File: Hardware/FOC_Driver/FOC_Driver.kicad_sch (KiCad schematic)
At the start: 0 parts

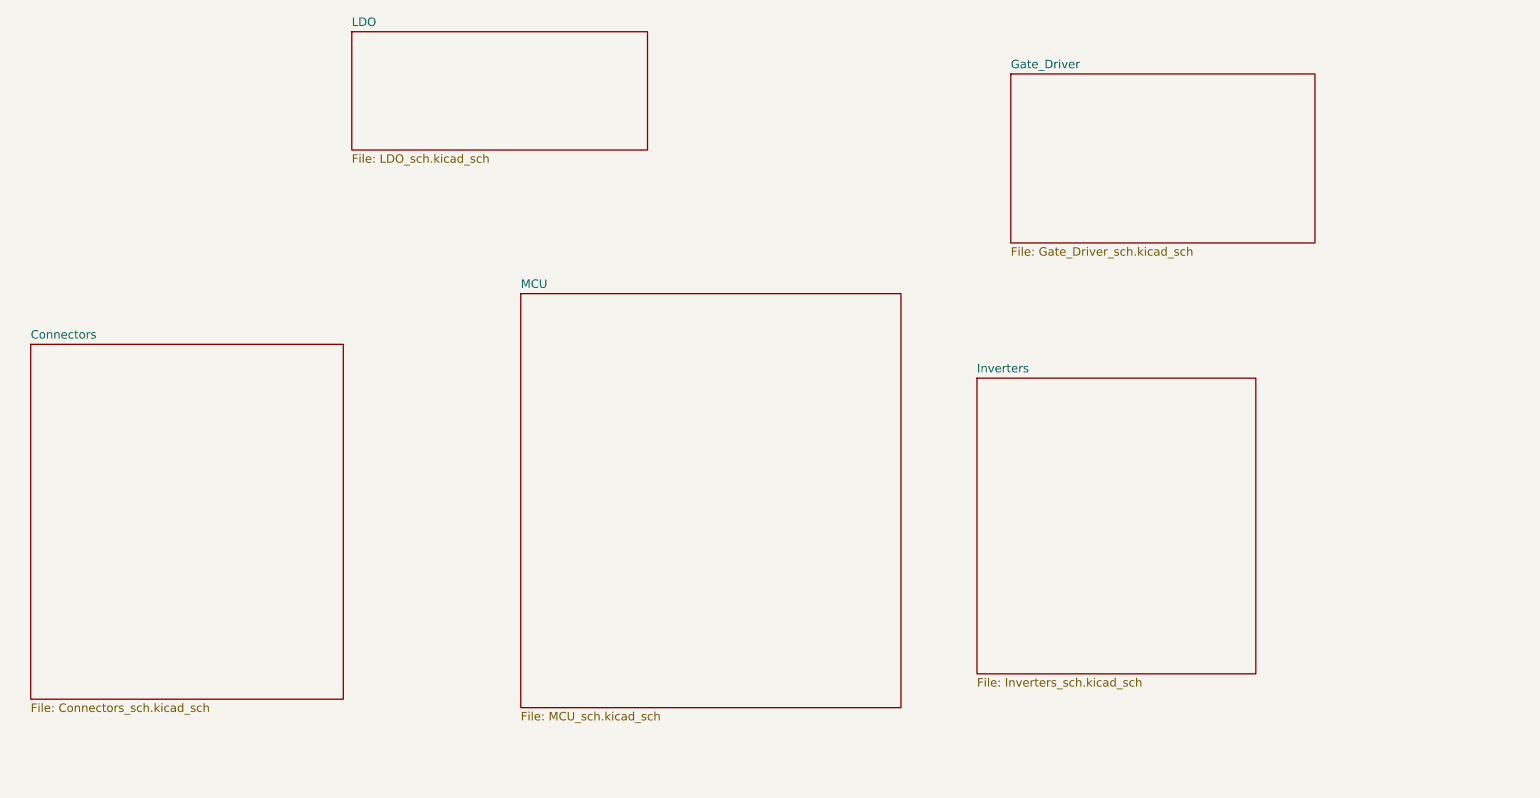
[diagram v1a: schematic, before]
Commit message: schematic completed
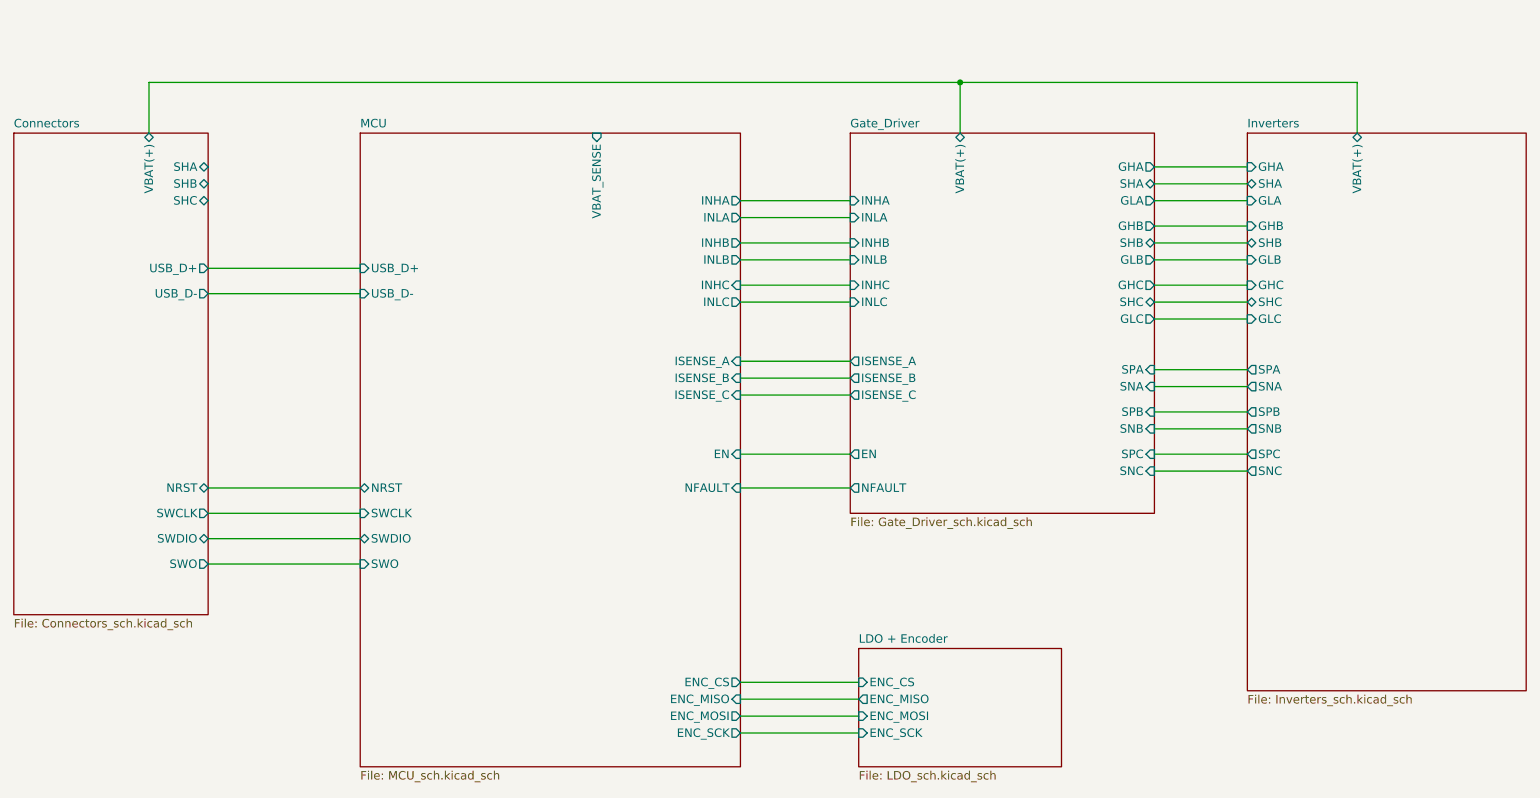
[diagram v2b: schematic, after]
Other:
- sheet LDO renamed LDO + Encoder
- sheet Connectors ports: added NRST, SHA, SHB, SHC, SWCLK, SWDIO, SWO, USB_D+, USB_D-, VBAT(+); removed none
- sheet Gate_Driver ports: added EN, GHA, GHB, GHC, GLA, GLB, GLC, INHA, INHB, INHC, INLA, INLB, INLC, ISENSE_A, ISENSE_B, ISENSE_C, NFAULT, SHA, SHB, SHC, SNA, SNB, SNC, SPA, SPB, SPC, VBAT(+); removed none
- sheet Inverters ports: added GHA, GHB, GHC, GLA, GLB, GLC, SHA, SHB, SHC, SNA, SNB, SNC, SPA, SPB, SPC, VBAT(+); removed none
- sheet LDO + Encoder ports: added ENC_CS, ENC_MISO, ENC_MOSI, ENC_SCK; removed none
- sheet MCU ports: added EN, ENC_CS, ENC_MISO, ENC_MOSI, ENC_SCK, INHA, INHB, INHC, INLA, INLB, INLC, ISENSE_A, ISENSE_B, ISENSE_C, NFAULT, NRST, SWCLK, SWDIO, SWO, USB_D+, USB_D-, VBAT_SENSE; removed none

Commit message: Schematic update, XT30/MR30 connectors and PCB layout in progress
- Connectors: AMASS XT30PW and MR30PW from Kicad_Libs (eConnector)
- Schematic updates on main, MCU and gate driver sheets
- PCB: footprints placed, routing in progress
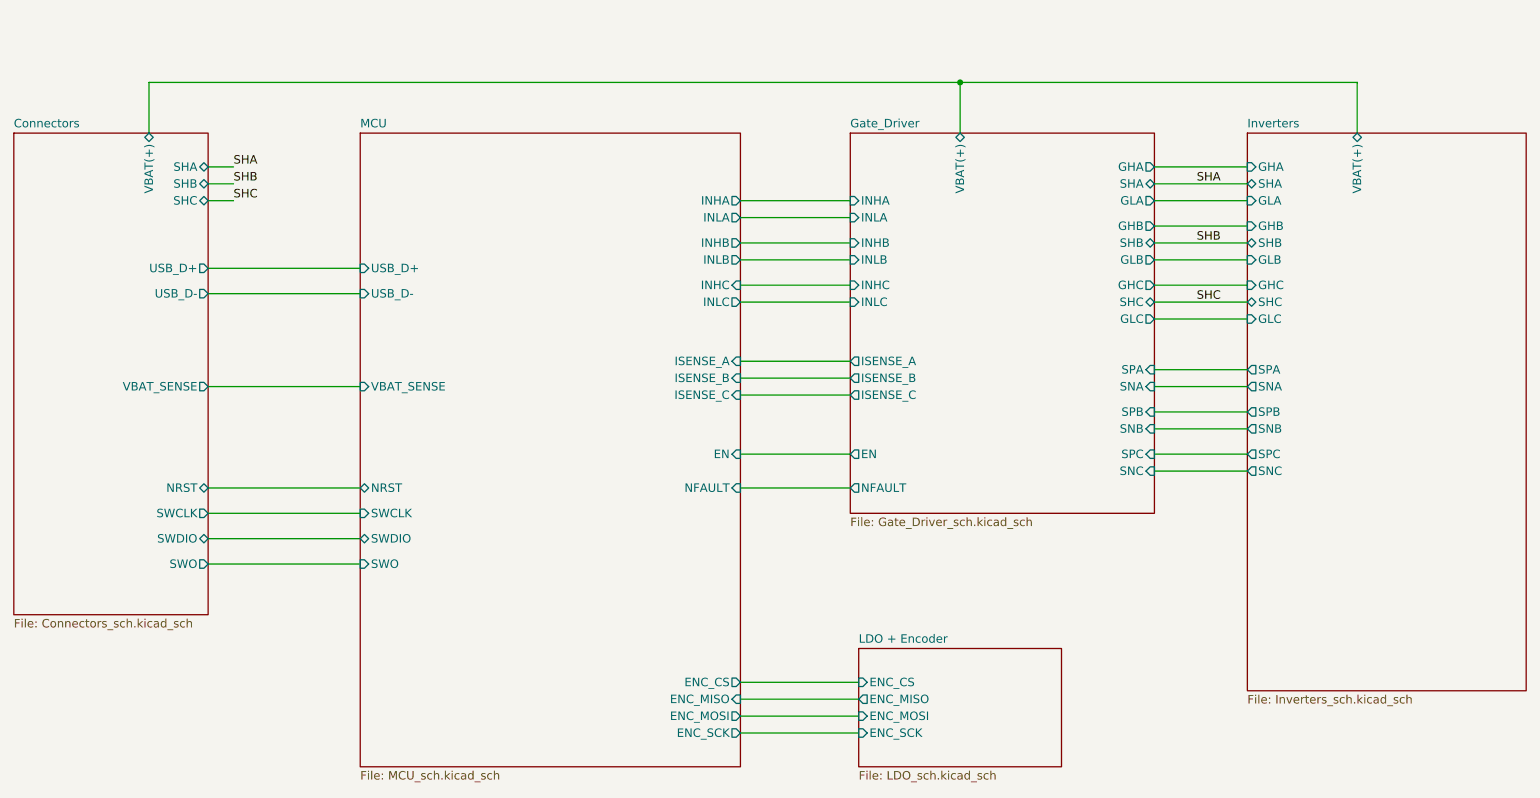
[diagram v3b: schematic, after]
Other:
- sheet Connectors ports: added VBAT_SENSE; removed none
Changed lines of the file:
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@@
 	(wire
 		(pts
+			(xy 63.5 85.09) (xy 86.36 85.09)
+		)
+		(stroke
+			(width 0)
+			(type default)
+		)
+	)
+	(wire
+		(pts
 			(xy 205.74 57.15) (xy 219.71 57.15)
 		)
@@
 	(wire
 		(pts
+			(xy 63.5 52.07) (xy 67.31 52.07)
+		)
+		(stroke
+			(width 0)
+			(type default)
+		)
+	)
+	(wire
+		(pts
 			(xy 176.53 46.99) (xy 176.53 39.37)
 		)
@@
 	(wire
 		(pts
+			(xy 63.5 57.15) (xy 67.31 57.15)
+		)
+		(stroke
+			(width 0)
+			(type default)
+		)
+	)
+	(wire
+		(pts
 			(xy 205.74 82.55) (xy 219.71 82.55)
 		)
@@
 	(wire
 		(pts
+			(xy 63.5 54.61) (xy 67.31 54.61)
+		)
+		(stroke
+			(width 0)
+			(type default)
+		)
+	)
+	(wire
+		(pts
 			(xy 63.5 100.33) (xy 86.36 100.33)
 		)
@@
 		)
 	)
+	(label "SHC"
+		(at 67.31 57.15 0)
+		(effects
+			(font
+				(size 1.27 1.27)
+			)
+			(justify left bottom)
+		)
+	)
+	(label "SHA"
+		(at 67.31 52.07 0)
+		(effects
+			(font
+				(size 1.27 1.27)
+			)
+			(justify left bottom)
+		)
+	)
+	(label "SHA"
+		(at 212.09 54.61 0)
+		(effects
+			(font
+				(size 1.27 1.27)
+			)
+			(justify left bottom)
+		)
+	)
+	(label "SHC"
+		(at 212.09 72.39 0)
+		(effects
+			(font
+				(size 1.27 1.27)
+			)
+			(justify left bottom)
+		)
+	)
+	(label "SHB"
+		(at 67.31 54.61 0)
+		(effects
+			(font
+				(size 1.27 1.27)
+			)
+			(justify left bottom)
+		)
+	)
+	(label "SHB"
+		(at 212.09 63.5 0)
+		(effects
+			(font
+				(size 1.27 1.27)
+			)
+			(justify left bottom)
+		)
+	)
 	(sheet
 		(at 160.02 46.99)
@@
 		)
 		(pin "VBAT_SENSE" input
-			(at 121.92 46.99 90)
+			(at 86.36 85.09 180)
 			(effects
 				(font
 					(size 1.27 1.27)
 				)
-				(justify right)
+				(justify left)
 			)
 		)
@@
 			(effects
 				(font
+					(size 1.27 1.27)
+				)
+				(justify right)
+			)
+		)
+		(pin "VBAT_SENSE" output
+			(at 63.5 85.09 0)
+			(effects
+				(font

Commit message: Layout completed
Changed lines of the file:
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@@
 			)
 		)
-		(pin "INHA" output
+		(pin "INHA" input
 			(at 143.51 57.15 0)
 			(effects
